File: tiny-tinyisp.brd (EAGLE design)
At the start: 48.6 x 12.7 mm, 17 parts, among them IC1 LDO-REGULATORMCP1801, Q1 NMOS, Q2 NMOS, Q3 NMOS, Q4 NMOS, U2 Tiny45

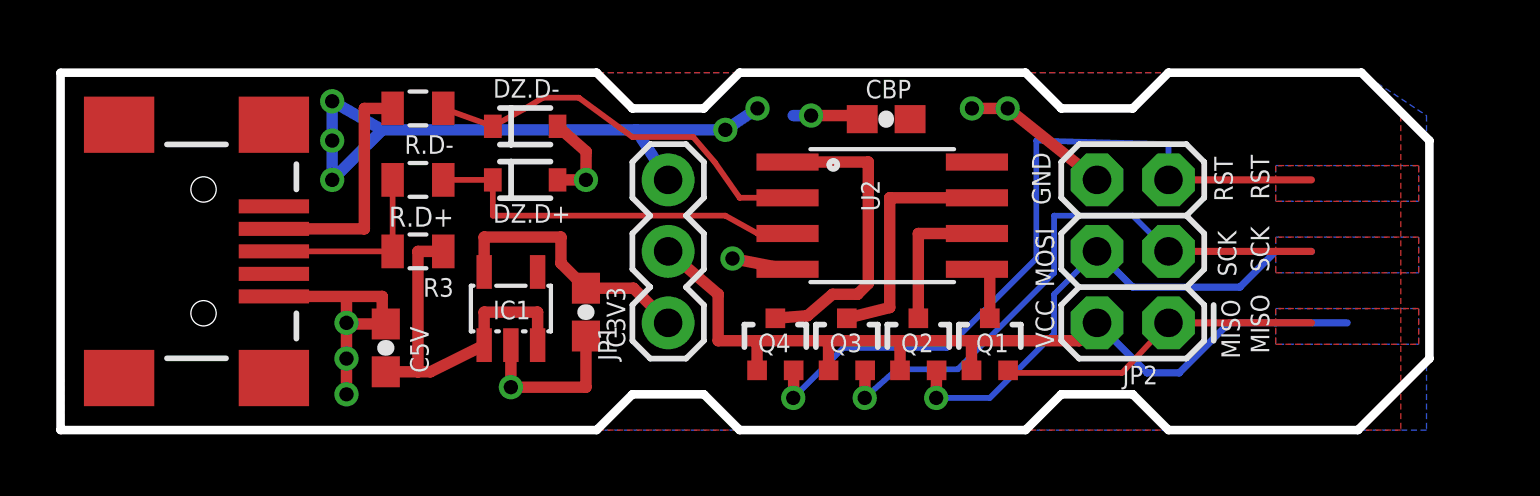
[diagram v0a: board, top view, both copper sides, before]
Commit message: Version 2 of the board
Fixed level-shifting diode on the wrong side

added in an option for HV reset
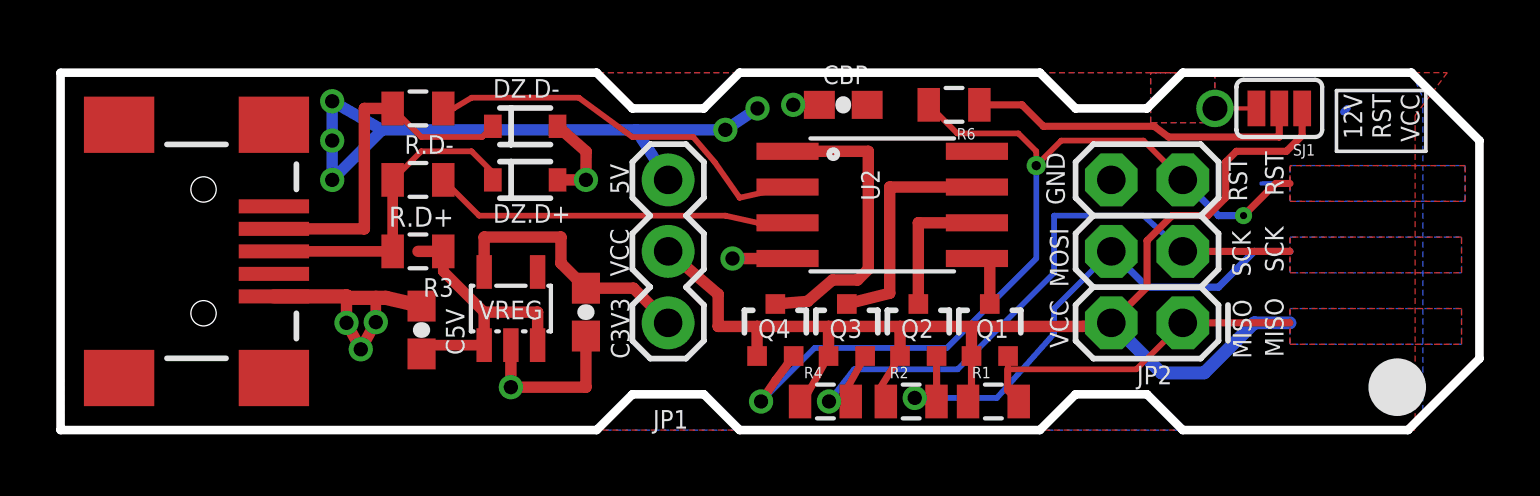
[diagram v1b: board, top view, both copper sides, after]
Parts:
- added HV_RST: TEST-POINT2, SparkFun-Passives:PAD.02X.02
- added R1, R2, R4, R6: (no value), SparkFun-Passives:0805
- added SJ1: (no value), SparkFun-Passives:SJ_3_PASTE1&2
- moved CBP 1.61 mm to (27.8, 24.3)
- moved C5V 1.42 mm to (12.8, 16.3)
- moved JP2 0.51 mm to (39.9, 16.5)
- moved Q1 0.51 mm to (33.0, 16.3)
- moved Q2 0.51 mm to (30.5, 16.3)
- moved Q3 0.51 mm to (27.9, 16.3)
- moved Q4 0.51 mm to (25.4, 16.3)
- moved U2 0.38 mm to (29.2, 20.7)
- renumbered IC1 to VREG
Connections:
- new net HVRST: HV_RST.P$1, SJ1.3
- new net N$1: R6.1, SJ1.2
- net D+: no longer DZ.D+.1
- net D-: no longer DZ.D-.1
- net J1.MISO: now also R1.2
- net J2.VCC: now also R1.1, R2.1, R4.1, SJ1.1
- net J3.SCK: now also R4.2
- net J4.MOSI: now also R2.2
- net J5.RST: now also R6.2
- net USB.D+: now also DZ.D+.1
- net USB.D-: now also DZ.D-.1
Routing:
- net J2.VCC: track 32.3 -> 47.2 mm
- net N$1: track 0.00 -> 12.1 mm
- net GND: track 29.0 -> 22.7 mm, vias 9 -> 7
- net J5.RST: track 26.9 -> 33.1 mm, vias 1 -> 3
- net USB.D+: track 6.76 -> 11.3 mm
- net USB.D-: track 8.50 -> 12.6 mm
- net VUSB: track 36.2 -> 33.5 mm
- net J3.SCK: track 21.2 -> 23.6 mm
- net HVRST: track 0.00 -> 1.47 mm, vias 0 -> 1
- net J4.MOSI: track 18.6 -> 19.6 mm
- net D+: track 13.7 -> 12.8 mm
- net J1.MISO: track 11.7 -> 12.5 mm
- added copper zone on layer 1, net HVRST
- added copper zone on layer 16, net HVRST
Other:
- board size 48.6 x 12.7 mm -> 50.4 x 12.7 mm
- board text added: "1"
- board text added: "12V"
- board text added: "2"
- board text added: "3"
- board text added: "4"
- board text added: "5"
- board text added: "5V"
- board text added: "F"
- board text added: "v2 05JAN2013"
- board text removed: "v1 25OCT2013"
